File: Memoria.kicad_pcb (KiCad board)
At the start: 2 copper layers, 242.9 x 96.6 mm, 136 parts, among them J1 RGB Breakout, J2 Hull LED Breakout, U1 PRTR5V0U2X, U2 ATmega32U4-MUR, Y1 16MHz

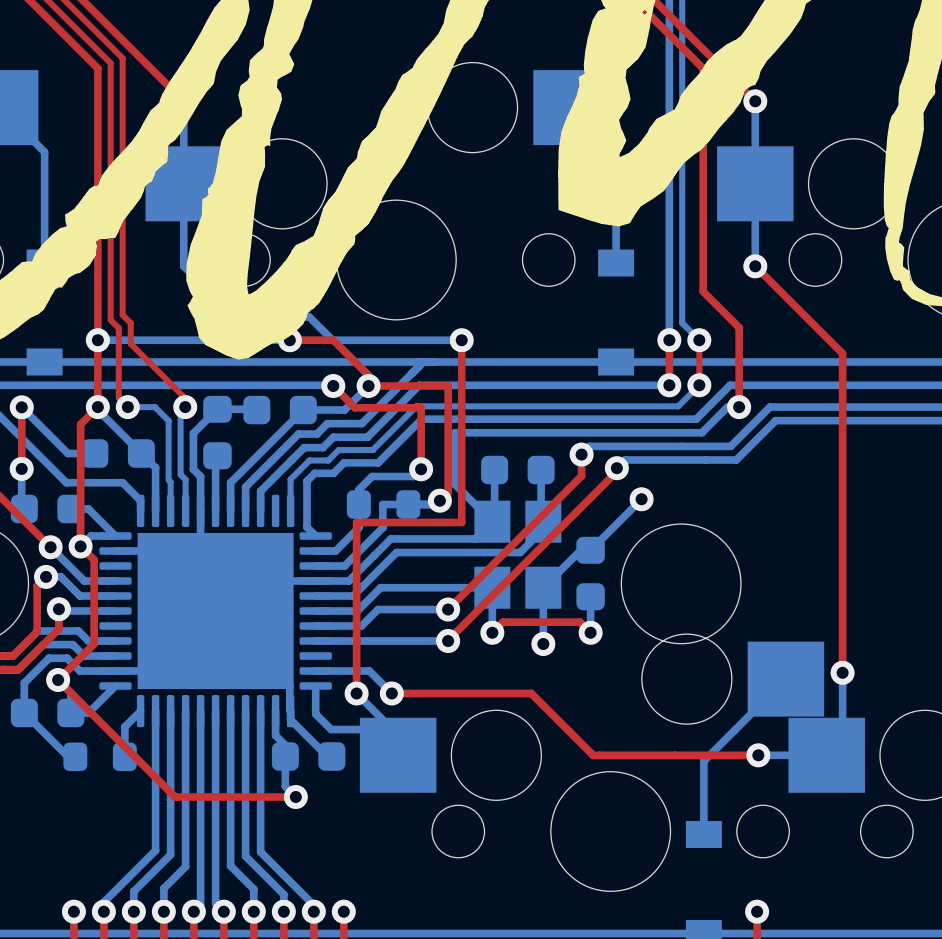
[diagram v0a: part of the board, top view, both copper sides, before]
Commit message: rerouted traces near crystal
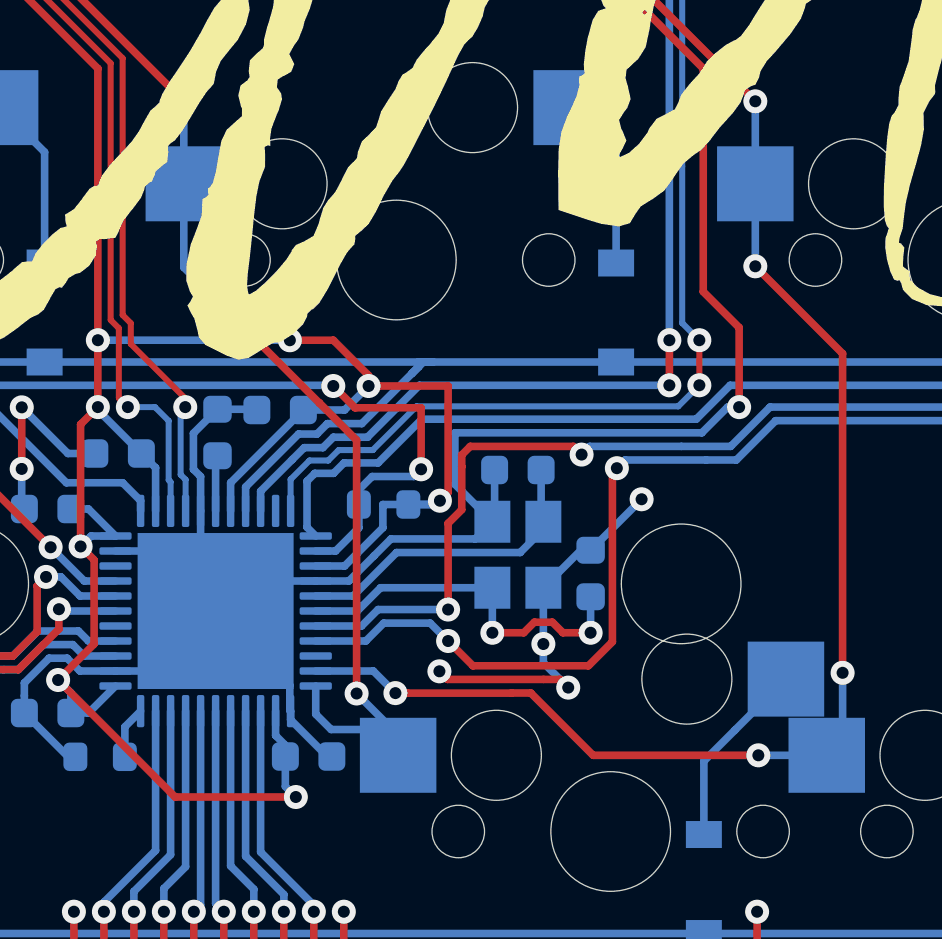
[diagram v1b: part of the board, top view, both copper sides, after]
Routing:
- net col5: track 102.2 -> 93.3 mm
- net GND: track 349.2 -> 355.5 mm, vias 40 -> 42
- net D1: track 135.8 -> 140.3 mm
- net row0: track 255.6 -> 258.2 mm

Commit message: final pass
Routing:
- net GND: vias 42 -> 41
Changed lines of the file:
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@@
       (drillshape 0)
       (scaleselection 1)
-      (outputdirectory "Gerbers/")
+      (outputdirectory "Gerbers/help/")
     )
   )
@@
   (via (at 32.04 48.073) (size 0.8) (drill 0.4) (layers "F.Cu" "B.Cu") (net 1))
   (via (at 127.4265 116.9735) (size 0.8) (drill 0.4) (layers "F.Cu" "B.Cu") (net 1))
-  (via (at 147.775 108.05) (size 0.8) (drill 0.4) (layers "F.Cu" "B.Cu") (net 1))
   (via (at 132.126988 116.9735) (size 0.8) (drill 0.4) (layers "F.Cu" "B.Cu") (net 1))
   (via (at 32.0422 44.3672) (size 0.8) (drill 0.4) (layers "F.Cu" "B.Cu") (net 1))
@@
   (segment (start 132.6125 110.35) (end 133.5125 109.45) (width 0.254) (layer "B.Cu") (net 2))
   (segment (start 145.337218 101.462782) (end 145.05352 101.74648) (width 0.254) (layer "F.Cu") (net 3))
-  (segment (start 149.05 101.73) (end 149.05 101.735762) (width 0.254) (layer "F.Cu") (net 3))
   (segment (start 57.655 46.101) (end 63.59 46.101) (width 0.254) (layer "F.Cu") (net 3))
   (segment (start 145.05352 101.74648) (end 145.05352 102.14) (width 0.254) (layer "F.Cu") (net 3))
-  (segment (start 148.77702 101.462782) (end 145.337218 101.462782) (width 0.254) (layer "F.Cu") (net 3))
   (segment (start 176.525 64.661374) (end 176.525 59.6989) (width 0.254) (layer "F.Cu") (net 3))
   (segment (start 144.6 104.027963) (end 144.6 106.90095) (width 0.254) (layer "F.Cu") (net 3))
   (segment (start 190.825 99.426511) (end 190.825 88.486374) (width 0.254) (layer "F.Cu") (net 3))
   (segment (start 181.194313 69.330687) (end 176.525 64.661374) (width 0.254) (layer "F.Cu") (net 3))
-  (segment (start 145.05352 102.14) (end 145.053531 102.140011) (width 0.254) (layer "F.Cu") (net 3))
+  (segment (start 148.77702 101.462782) (end 145.337218 101.462782) (width 0.254) (layer "F.Cu") (net 3))
   (segment (start 190.825 88.486374) (end 181.194313 78.855687) (width 0.254) (layer "F.Cu") (net 3))
+  (segment (start 145.05352 102.14) (end 145.053531 102.140011) (width 0.254) (layer "F.Cu") (net 3))
   (segment (start 145.053531 102.140011) (end 145.053531 103.574432) (width 0.254) (layer "F.Cu") (net 3))
-  (segment (start 181.194313 78.855687) (end 181.194313 69.330687) (width 0.254) (layer "F.Cu") (net 3))
   (segment (start 149.05 101.735762) (end 148.77702 101.462782) (width 0.254) (layer "F.Cu") (net 3))
+  (segment (start 181.194313 78.855687) (end 181.194313 69.330687) (width 0.254) (layer "F.Cu") (net 3))
   (segment (start 145.053531 103.574432) (end 144.6 104.027963) (width 0.254) (layer "F.Cu") (net 3))
   (via (at 190.825 99.426511) (size 0.8) (drill 0.4) (layers "F.Cu" "B.Cu") (net 3))
@@
   (via (at 131.0275 38.31) (size 0.8) (drill 0.4) (layers "F.Cu" "B.Cu") (net 62))
   (via (at 126.265 76.41) (size 0.8) (drill 0.4) (layers "F.Cu" "B.Cu") (net 62))
+  (segment (start 135.79 95.497) (end 137.49 97.197) (width 0.254) (layer "B.Cu") (net 62))
   (segment (start 140.1875 110.3875) (end 140.7 110.9) (width 0.254) (layer "B.Cu") (net 62))
   (segment (start 131.0275 35.56) (end 131.0275 38.31) (width 0.254) (layer "B.Cu") (net 62))
-  (segment (start 135.79 92.71) (end 135.79 95.497) (width 0.254) (layer "B.Cu") (net 62))
   (segment (start 126.265 73.66) (end 126.265 70.91) (width 0.254) (layer "B.Cu") (net 62))
-  (segment (start 135.79 95.497) (end 137.49 97.197) (width 0.254) (layer "B.Cu") (net 62))
   (segment (start 121.5025 54.61) (end 121.5025 57.36) (width 0.254) (layer "B.Cu") (net 62))
   (segment (start 140.7 110.9) (end 142.07375 110.9) (width 0.254) (layer "B.Cu") (net 62))
@@
   (segment (start 121.5025 54.61) (end 121.5025 51.86) (width 0.254) (layer "B.Cu") (net 62))
   (segment (start 142.07375 110.9) (end 142.93375 111.76) (width 0.254) (layer "B.Cu") (net 62))
+  (segment (start 135.79 92.71) (end 135.79 95.497) (width 0.254) (layer "B.Cu") (net 62))
   (segment (start 135.79 92.71) (end 135.79 89.96) (width 0.254) (layer "B.Cu") (net 62))
   (segment (start 126.265 73.66) (end 126.265 76.41) (width 0.254) (layer "B.Cu") (net 62))
@@
   (segment (start 48.004 32.229) (end 46.5 30.725) (width 0.254) (layer "B.Cu") (net 71))
   (segment (start 247.65 80.94) (end 247.65 85.8) (width 0.254) (layer "F.Cu") (net 72))
-  (segment (start 144.6 107.95) (end 144.6 107.928393) (width 0.254) (layer "F.Cu") (net 72))
   (segment (start 149.275932 108.776511) (end 145.426511 108.776511) (width 0.254) (layer "F.Cu") (net 72))
   (segment (start 150.225 102.189282) (end 150.076511 102.337771) (width 0.254) (layer "F.Cu") (net 72))
@@
   (segment (start 250.899928 84.189928) (end 247.65 80.94) (width 0.254) (layer "B.Cu") (net 72))
   (segment (start 175.438352 100.153022) (end 174.986343 100.605031) (width 0.254) (layer "B.Cu") (net 72))
-  (segment (start 144.579437 107.95) (end 144.6 107.95) (width 0.254) (layer "B.Cu") (net 72))
   (segment (start 154.207386 101.916302) (end 153.2 101.916302) (width 0.254) (layer "B.Cu") (net 72))
   (segment (start 252.4125 84.19) (end 250.899928 84.19) (width 0.254) (layer "B.Cu") (net 72))
@@
         (xy 150.241 108.298)
         (xy 148.175 108.298)
-        (xy 148.175 107.65)
-        (xy 147.375 107.65)
         (xy 147.375 108.298)
         (xy 145.275 108.298)
